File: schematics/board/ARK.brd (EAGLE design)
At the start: 89.6 x 89 mm, 215 parts, among them IC1 STM32F103C8T, Q5 8MHz

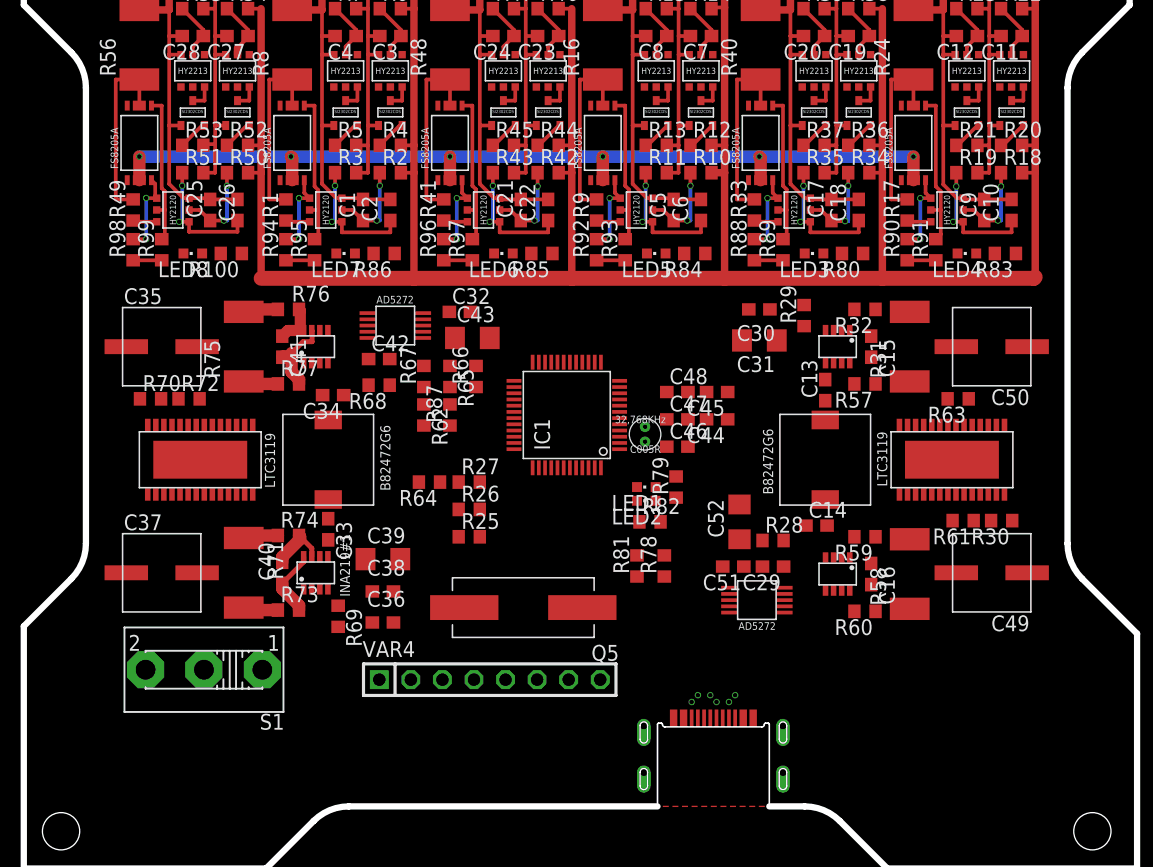
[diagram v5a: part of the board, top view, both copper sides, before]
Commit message: В плате АРК разведены дорожки групп BMS и всех DC-DC. Остался МК и его обвес
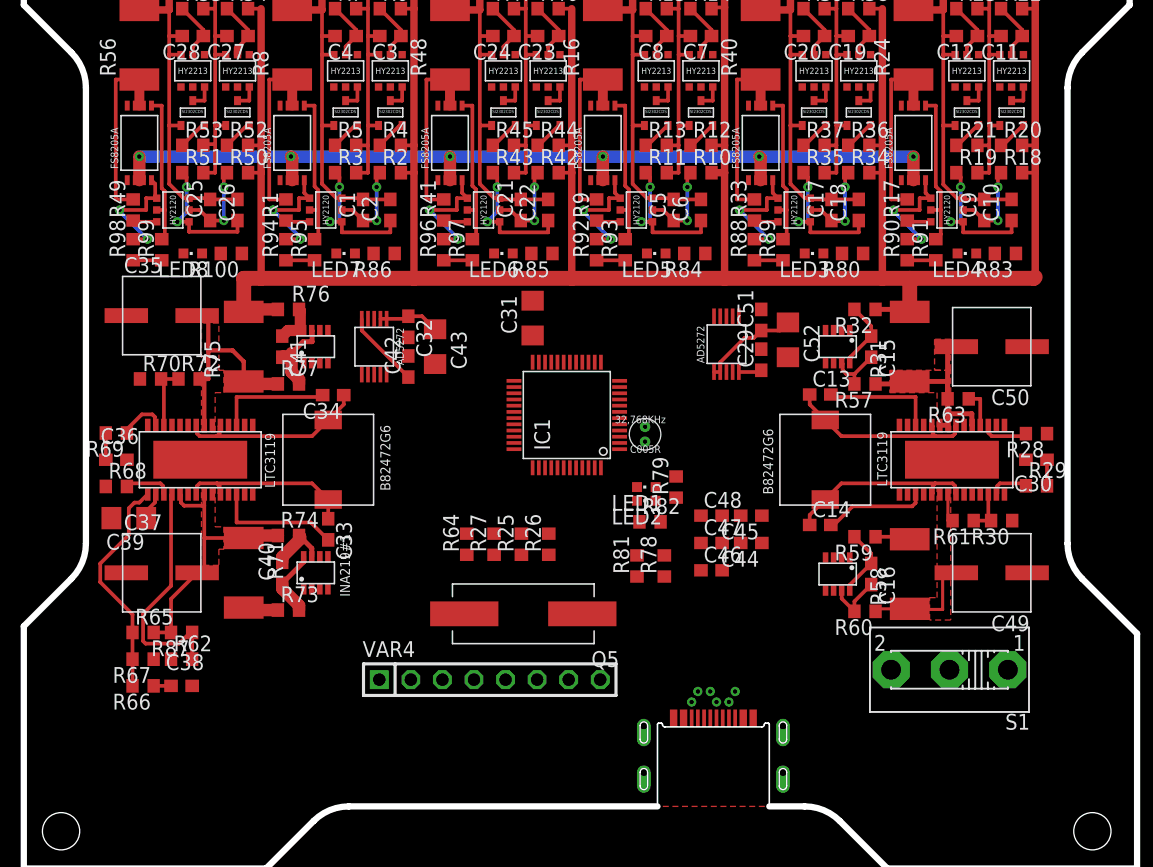
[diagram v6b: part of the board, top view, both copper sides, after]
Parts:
- removed U$22: AD5272, CanCubeSat:AD5272
- added AD5272#2: AD5272, CanCubeSat:AD5272
- moved S1 60.0 mm to (74.5, 16.0)
- moved R66 36.6 mm to (9.60, 14.7), turned to 180 degrees
- moved R65 32.2 mm to (9.60, 19.0), turned to 0 degrees
- moved R67 32.1 mm to (9.60, 16.9), turned to 180 degrees
- moved R87 27.8 mm to (12.7, 19.0), turned to 180 degrees
- moved R62 27.7 mm to (12.7, 16.9), turned to 0 degrees
- moved C30 25.4 mm to (81.5, 32.9)
- moved C36 25.1 mm to (7.45, 32.9)
- moved R29 23.2 mm to (81.5, 30.8), turned to 0 degrees
- moved R69 23.2 mm to (7.45, 35.0), turned to 180 degrees
- moved R28 22.9 mm to (81.5, 35.0), turned to 180 degrees
- moved R68 22.7 mm to (7.45, 30.8), turned to 0 degrees
- moved C39 20.7 mm to (8.45, 28.2), turned to 180 degrees
- moved C51 20.0 mm to (59.4, 44.1), turned to 90 degrees
- moved C31 18.3 mm to (41.0, 44.3), turned to 90 degrees
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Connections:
- net DPD_RST: now also AD5272#2.7; no longer U$22.7
- net GND: now also AD5272#2.10, AD5272#2.3, AD5272#2.4, AD5272#2.6; no longer U$22.10, U$22.3, U$22.4, U$22.6
- net N$5: now also AD5272#2.1, AD5272#2.2; no longer U$22.1, U$22.2
- net N$51: now also AD5272#2.5; no longer U$22.5
- net SCL: now also AD5272#2.9; no longer U$22.9
- net SDA: now also AD5272#2.8; no longer U$22.8
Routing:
- net N$137: track 2.83 -> 22.7 mm
- net N$55: track 0.00 -> 19.3 mm
- net 90: track 0.00 -> 18.3 mm
- net N$14: track 0.00 -> 18.0 mm
- net N$134: track 2.83 -> 18.5 mm
- net N$132: track 0.00 -> 15.4 mm
- net N$12: track 0.00 -> 15.3 mm
- net N$11: track 0.00 -> 15.3 mm
- net N$131: track 0.00 -> 14.4 mm
- net N$50: track 0.00 -> 12.2 mm
- net N$144: track 0.00 -> 10.2 mm
- net BMS+: track 231.8 -> 241.5 mm
- net N$32: track 0.00 -> 9.30 mm
- net N$129: track 0.00 -> 9.26 mm
- net N$52: track 0.00 -> 8.26 mm
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- added copper zone on layer 1, net N$134
- added copper zone on layer 1, net N$137
- added copper zone on layer 1, net N$14
- added copper zone on layer 1, net N$50

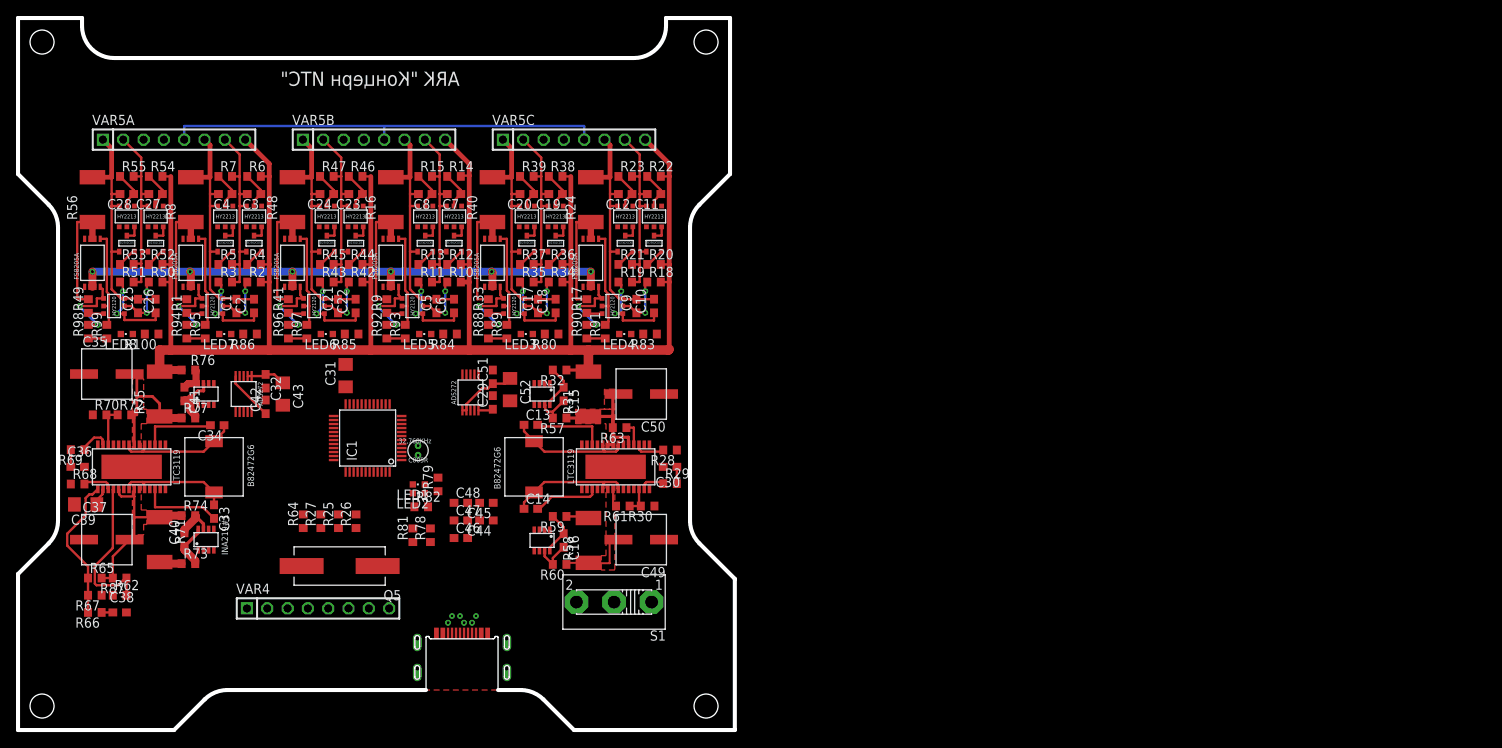
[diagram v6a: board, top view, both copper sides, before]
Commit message: В плате АРК разведено еще больше дорожек - до 99%. Надо заменить МК или подключить текущий МК к GND
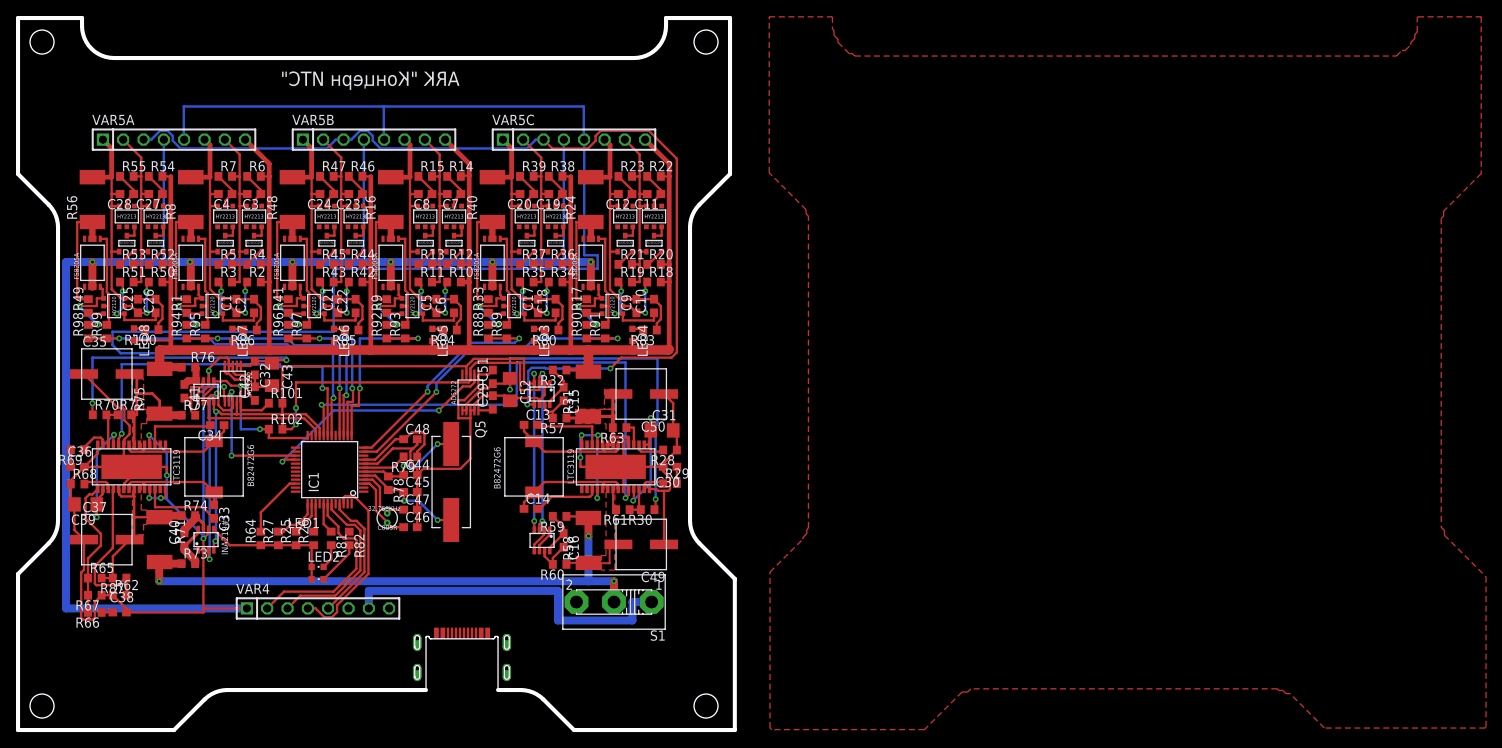
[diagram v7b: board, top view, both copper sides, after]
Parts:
- added R101, R102: 4k7, resistor:R0603
- moved C31 40.1 mm to (80.5, 37.5), turned to 0 degrees
- moved Q5 17.5 mm to (54.1, 31.0), turned to 270 degrees
- moved LED1 17.3 mm to (37.5, 18.9), turned to 270 degrees
- moved LED2 15.6 mm to (37.5, 20.4), turned to 270 degrees
- moved C44 11.1 mm to (49.0, 31.9), turned to 0 degrees
- moved R81 10.2 mm to (39.1, 23.9), turned to 270 degrees
- moved C48 10.1 mm to (49.0, 36.4)
- moved R82 9.83 mm to (41.4, 23.9), turned to 270 degrees
- moved C45 9.60 mm to (49.0, 29.8), turned to 0 degrees
- moved C005R 9.29 mm to (46.1, 26.5)
- moved R78 8.36 mm to (46.3, 30.9), turned to 270 degrees
- moved C46 6.44 mm to (49.0, 25.4)
- moved C47 6.44 mm to (49.0, 27.6)
- moved IC1 6.18 mm to (39.0, 32.5)
- moved R27 5.72 mm to (32.5, 23.9)
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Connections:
- new net N$26: C31.1, U$16.11, U$16.15, U$16.16
- net BMS+: now also LED3.C, LED4.C, LED5.C, LED6.C, LED7.C, LED8.C
- net BMS1: now also IC1.15; no longer IC1.11
- net BMS2: now also IC1.16; no longer IC1.12
- net BMS5: now also IC1.11; no longer IC1.15
- net BMS6: now also IC1.12; no longer IC1.16
- net BUSPLUS: no longer LED3.C, LED4.C, LED5.C, LED6.C, LED7.C, LED8.C
- net SCL: now also R101.2
- net SDA: now also R102.2
- net VDD: now also R101.1, R102.1; no longer C31.1, U$16.11, U$16.15, U$16.16
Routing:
- net GND: track 73.8 -> 468.5 mm, vias 6 -> 17
- net VDD: track 0.00 -> 186.8 mm, vias 2 -> 4
- net 1W: track 55.1 -> 189.1 mm, vias 0 -> 1
- net SDA: track 0.00 -> 111.6 mm, vias 0 -> 6
- net SCL: track 0.00 -> 98.1 mm, vias 0 -> 4
- net BUS+: track 5.78 -> 75.6 mm, vias 0 -> 3
- net PGOOD2: track 0.00 -> 65.6 mm, vias 0 -> 2
- net PGOOD1: track 0.00 -> 45.0 mm, vias 0 -> 2
- net BUSPLUS: track 0.00 -> 43.6 mm
- net N$5: track 8.06 -> 51.1 mm, vias 0 -> 2
- net BMS2: track 2.30 -> 42.8 mm, vias 0 -> 2
- net BMS5: track 2.30 -> 42.1 mm, vias 0 -> 2
- net N$25: track 4.92 -> 38.4 mm, vias 0 -> 2
- net DPD_RST: track 0.00 -> 30.8 mm, vias 0 -> 2
- net BMS1: track 2.30 -> 32.0 mm, vias 0 -> 2
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
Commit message: Разведена плата АРК
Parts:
- removed IC1: STM32F103C8T, micro-stm:LQFP48
- added IC2: STM32F103C8T, CanCubeSat:LQFP48
- R101, R102: value 4k7 -> 5k1
- moved R25 0.62 mm to (34.8, 23.3)
- moved R26 0.62 mm to (37.0, 23.3)
- moved R27 0.62 mm to (32.5, 23.3)
- moved R64 0.62 mm to (30.4, 23.3)
- moved R81 0.62 mm to (39.1, 23.3)
- moved R82 0.62 mm to (41.4, 23.3)
- moved C35 0.53 mm to (11.0, 44.0)
- moved R70 0.53 mm to (10.1, 38.9)
- moved R72 0.53 mm to (13.2, 38.9)
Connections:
- removed net VSS: IC1.23, IC1.35, IC1.47
- net 1W: now also IC2.18; no longer IC1.18
- net BMS1: now also IC2.15; no longer IC1.15
- net BMS2: now also IC2.16; no longer IC1.16
- net BMS3: now also IC2.13; no longer IC1.13
- net BMS4: now also IC2.14; no longer IC1.14
- net BMS5: now also IC2.11; no longer IC1.11
- net BMS6: now also IC2.12; no longer IC1.12
- net DPC_RST: now also IC2.27; no longer IC1.27
- net DPD_RST: now also IC2.28; no longer IC1.28
- net GND: now also IC2.23, IC2.35, IC2.47, IC2.8; no longer IC1.8
- net I2CINT: now also IC2.43; no longer IC1.43
- net N$133: now also IC2.6; no longer IC1.6
- net N$145: now also IC2.5; no longer IC1.5
- net N$148: now also IC2.4; no longer IC1.4
- net N$152: now also IC2.3; no longer IC1.3
- net N$156: now also IC2.38; no longer IC1.38
- net N$157: now also IC2.39; no longer IC1.39
- net N$161: now also IC2.41; no longer IC1.41
- net NRST: now also IC2.7; no longer IC1.7
- net PGOOD1: now also IC2.19; no longer IC1.19
- net PGOOD2: now also IC2.20; no longer IC1.20
- net RX-C: now also IC2.31; no longer IC1.31
- net SCL: now also IC2.21; no longer IC1.21
- net SCLTM: now also IC2.45; no longer IC1.45
- net SDA: now also IC2.22; no longer IC1.22
- net SDATM: now also IC2.46; no longer IC1.46
- net SWC: now also IC2.37; no longer IC1.37
- net SWD: now also IC2.34; no longer IC1.34
- net TIME: now also IC2.42; no longer IC1.42
- net TX-C: now also IC2.30; no longer IC1.30
- net VBAT: now also IC2.1; no longer IC1.1
- net VDD: now also IC2.24, IC2.36, IC2.48, IC2.9; no longer IC1.24, IC1.36, IC1.48, IC1.9
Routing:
- net GND: track 468.5 -> 614.8 mm, vias 17 -> 24
- net VDD: track 186.8 -> 304.9 mm, vias 4 -> 11
- net TX-C: track 0.00 -> 40.0 mm, vias 0 -> 2
- net RX-C: track 0.00 -> 37.9 mm, vias 0 -> 2
- net SWD: track 8.24 -> 43.6 mm, vias 0 -> 2
- net SWC: track 5.89 -> 39.9 mm, vias 0 -> 2
- net NRST: track 5.56 -> 29.8 mm, vias 0 -> 2
- net SCLTM: track 16.7 -> 19.5 mm
- net I2CINT: track 21.5 -> 23.9 mm
- net SDATM: track 23.4 -> 24.6 mm
- net N$161: track 3.89 -> 4.55 mm
- net TIME: track 23.7 -> 24.3 mm
- net N$17: track 3.09 -> 2.47 mm
- net N$159: track 5.58 -> 4.96 mm
- net N$157: track 3.60 -> 4.22 mm
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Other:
- board text added: "BMS"
- board text added: "Charge DC-DC"
- board text added: "Discharge DC-DC"
